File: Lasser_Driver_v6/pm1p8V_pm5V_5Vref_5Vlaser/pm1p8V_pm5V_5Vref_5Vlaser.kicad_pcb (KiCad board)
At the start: 2 copper layers, 160 x 100 mm, 103 parts, among them J6 DIN41612_M_3x8+8_Power_Male, U1 MC7808CTG, U10 LT3042EMSE +14.3V, U13 MC7812CTG, U14 MC7808CTG, U15 LT3045EMSE 5V, U16 LT3045EMSE 5V, U17 MC7808CTG, U18 MC7906CTG, U19 LT3045EMSE 5V, U2 LT3042EMSE +5.5V, U20 LT3094EMSE -5V, U21 OPA192IDBVR, U3 LTC6655BHMS8-5#PBF, U4 MC7812CTG, U5 MC7805CTG, U6 LT3045EMSE 3.3V, U7 LP5907MFX-1.8, U8 TPS7A3901DSCR, U9 LT3094EMSE -14.3V

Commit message: Main updates to CH card v6
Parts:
- R42, R43: value 20m PCB Trace -> 20m 1%
- moved C73 8.01 mm to (91.5, 135.8), turned to 180 degrees
- moved C75 0.50 mm to (94.4, 136.8)
- moved R49 0.50 mm to (97.0, 136.8)
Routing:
- net -15V: track 59.9 -> 65.4 mm
- net Net-(U21-IN-): track 2.75 -> 5.29 mm
- net GND: vias 267 -> 270
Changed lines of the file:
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@@
 		(tags "resistor handsolder")
 		(property "Reference" "R50"
-			(at 0 -1.65 0)
+			(at 0.2 1.6 180)
 			(layer "F.SilkS")
 			(effects
@@
 			(unit
 				(name "A")
-				(pins "3" "2" "5" "4" "1")
+				(pins "3" "4" "5" "2" "1")
 			)
 		)
@@
 	(footprint "Capacitor_SMD:C_0805_2012Metric_Pad1.18x1.45mm_HandSolder"
 		(layer "F.Cu")
-		(at 94.9625 128.55)
+		(at 91.4625 135.75 180)
 		(descr "Capacitor SMD 0805 (2012 Metric), square (rectangular) end terminal, IPC-7351 nominal with elongated pad for handsoldering. (Body size source: IPC-SM-782 page 76, https://www.pcb-3d.com/wordpress/wp-content/uploads/ipc-sm-782a_amendment_1_and_2.pdf, https://docs.google.com/spreadsheets/d/1BsfQQcO9C6DZCsRaXUlFlo91Tg2WpOkGARC1WS5S8t0/edit?usp=sharing)")
 		(tags "capacitor handsolder")
@@
 		)
 		(property "Manufacturer Part Number" "CL21B104KBCNNNC"
-			(at 0 0 0)
+			(at 0 0 180)
 			(unlocked yes)
 			(layer "F.Fab")
@@
 		)
 		(property "Manufacturer" "Samsung Electro-Mechanics"
-			(at 0 0 0)
+			(at 0 0 180)
 			(unlocked yes)
 			(layer "F.Fab")
@@
 		)
 		(property "DigiKey P/N" "1276-1003-2-ND"
-			(at 0 0 0)
+			(at 0 0 180)
 			(unlocked yes)
 			(layer "F.Fab")
@@
 		(duplicate_pad_numbers_are_jumpers no)
 		(fp_line
-			(start -0.261252 -0.735)
-			(end 0.261252 -0.735)
+			(start -0.261252 0.735)
+			(end 0.261252 0.735)
 			(stroke
 				(width 0.12)
@@
 		)
 		(fp_line
-			(start -0.261252 0.735)
-			(end 0.261252 0.735)
+			(start -0.261252 -0.735)
+			(end 0.261252 -0.735)
 			(stroke
 				(width 0.12)
@@
 		)
 		(pad "1" smd roundrect
-			(at -1.0375 0)
+			(at -1.0375 0 180)
 			(size 1.175 1.45)
 			(layers "F.Cu" "F.Mask" "F.Paste")
@@
 		)
 		(pad "2" smd roundrect
-			(at 1.0375 0)
+			(at 1.0375 0 180)
 			(size 1.175 1.45)
 			(layers "F.Cu" "F.Mask" "F.Paste")
@@
 			)
 		)
-		(property "Value" "20m PCB Trace"
+		(property "Value" "20m 1%"
 			(at 0 1.65 0)
 			(layer "F.Fab")
@@
 			)
 		)
+		(property "Manufacturer Part Number" "ERJ-6BWFR020V"
+			(at 0 0 180)
+			(unlocked yes)
+			(layer "F.Fab")
+			(hide yes)
+			(effects
+				(font
+					(size 1 1)
+					(thickness 0.15)
+				)
+			)
+		)
+		(property "Manufacturer" "Panasonic Industry"
+			(at 0 0 180)
+			(unlocked yes)
+			(layer "F.Fab")
+			(hide yes)
+			(effects
+				(font
+					(size 1 1)
+					(thickness 0.15)
+				)
+			)
+		)
+		(property "DigiKey P/N" "P.02AQTR-ND"
+			(at 0 0 180)
+			(unlocked yes)
+			(layer "F.Fab")
+			(hide yes)
+			(effects
+				(font
+					(size 1 1)
+					(thickness 0.15)
+				)
+			)
+		)
 		(sheetname "/")
 		(sheetfile "pm1p8V_pm5V_5Vref_5Vlaser.kicad_sch")
@@
 			)
 		)
-		(attr smd dnp)
+		(attr smd)
 		(duplicate_pad_numbers_are_jumpers no)
 		(fp_line
@@
 			)
 		)
-		(property "Value" "20m PCB Trace"
+		(property "Value" "20m 1%"
 			(at 0 1.65 0)
 			(layer "F.Fab")
@@
 			)
 		)
+		(property "Manufacturer Part Number" "ERJ-6BWFR020V"
+			(at 0 0 180)
+			(unlocked yes)
+			(layer "F.Fab")
+			(hide yes)
+			(effects
+				(font
+					(size 1 1)
+					(thickness 0.15)
+				)
+			)
+		)
+		(property "Manufacturer" "Panasonic Industry"
+			(at 0 0 180)
+			(unlocked yes)
+			(layer "F.Fab")
+			(hide yes)
+			(effects
+				(font
+					(size 1 1)
+					(thickness 0.15)
+				)
+			)
+		)
+		(property "DigiKey P/N" "P.02AQTR-ND"
+			(at 0 0 180)
+			(unlocked yes)
+			(layer "F.Fab")
+			(hide yes)
+			(effects
+				(font
+					(size 1 1)
+					(thickness 0.15)
+				)
+			)
+		)
 		(sheetname "/")
 		(sheetfile "pm1p8V_pm5V_5Vref_5Vlaser.kicad_sch")
@@
 			)
 		)
-		(attr smd dnp)
+		(attr smd)
 		(duplicate_pad_numbers_are_jumpers no)
 		(fp_line
@@
 	(footprint "Capacitor_SMD:C_0805_2012Metric_Pad1.18x1.45mm_HandSolder"
 		(layer "F.Cu")
-		(at 93.9 136.8125 -90)
+		(at 94.4 136.8125 -90)
 		(descr "Capacitor SMD 0805 (2012 Metric), square (rectangular) end terminal, IPC-7351 nominal with elongated pad for handsoldering. (Body size source: IPC-SM-782 page 76, https://www.pcb-3d.com/wordpress/wp-content/uploads/ipc-sm-782a_amendment_1_and_2.pdf, https://docs.google.com/spreadsheets/d/1BsfQQcO9C6DZCsRaXUlFlo91Tg2WpOkGARC1WS5S8t0/edit?usp=sharing)")
 		(tags "capacitor handsolder")
@@
 	(footprint "Resistor_SMD:R_0805_2012Metric_Pad1.20x1.40mm_HandSolder"
 		(layer "F.Cu")
-		(at 96.5 136.75 90)
+		(at 97 136.75 90)
 		(descr "Resistor SMD 0805 (2012 Metric), square (rectangular) end terminal, IPC-7351 nominal with elongated pad for handsoldering. (Body size source: IPC-SM-782 page 72, https://www.pcb-3d.com/wordpress/wp-content/uploads/ipc-sm-782a_amendment_1_and_2.pdf)")
 		(tags "resistor handsolder")
@@
 		(tags "capacitor handsolder")
 		(property "Reference" "C18"
-			(at 3.4375 0 90)
+			(at -0.8125 -1.65 90)
 			(layer "F.SilkS")
 			(effects
@@
 	)
 	(via
-		(at 91.5 140.1)
+		(at 94.4 139.4)
 		(size 0.8)
 		(drill 0.4)
@@
 	)
 	(via
+		(at 90.45 137.55)
+		(size 0.8)
+		(drill 0.4)
+		(layers "F.Cu" "B.Cu")
+		(free yes)
+		(net "GND")
+	)
+	(via
 		(at 203.8 107.5)
 		(size 0.8)
@@
 	)
 	(via
+		(at 90.45 126.65)
+		(size 0.8)
+		(drill 0.4)
+		(layers "F.Cu" "B.Cu")
+		(free yes)
+		(net "GND")
+	)
+	(via
 		(at 90.7 51.8)
 		(size 0.8)
@@
 	)
 	(via
-		(at 98.2 138.6)
+		(at 98.8 139.1)
 		(size 0.8)
 		(drill 0.4)
@@
 	)
 	(via
-		(at 96.5 139.6)
+		(at 97 139.3)
 		(size 0.8)
 		(drill 0.4)
@@
 	)
 	(via
+		(at 88.85 136)
+		(size 0.8)
+		(drill 0.4)
+		(layers "F.Cu" "B.Cu")
+		(free yes)
+		(net "GND")
+	)
+	(via
 		(at 152.8 107.7)
 		(size 0.8)
@@
 	)
 	(via
-		(at 93.9 139.6)
+		(at 95.75 137.8)
 		(size 0.8)
 		(drill 0.4)
@@
 	)
 	(via
-		(at 92.1 137.8)
+		(at 95.75 139.35)
 		(size 0.8)
 		(drill 0.4)
@@
 	)
 	(segment
-		(start 93.925 128.55)
-		(end 93.925 130.725)
-		(width 1)
-		(layer "F.Cu")
-		(net "-15V")
-	)
-	(segment
-		(start 93.1 126.4)
-		(end 85.2 126.4)
-		(width 1)
-		(layer "F.Cu")
-		(net "-15V")
-	)
-	(segment
 		(start 74.035 115.115)
 		(end 74.035 115.765)
@@
 	)
 	(segment
-		(start 85.2 126.4)
-		(end 84.5 125.7)
-		(width 1)
-		(layer "F.Cu")
-		(net "-15V")
-	)
-	(segment
-		(start 93.925 130.725)
-		(end 93.9 130.75)
+		(start 58.4 102.8)
+		(end 59.86 101.34)
 		(width 1)
 		(layer "F.Cu")
@@
 	)
 	(segment
-		(start 58.4 102.8)
-		(end 59.86 101.34)
+		(start 71.8 116.4)
+		(end 74.02 116.4)
 		(width 1)
 		(layer "F.Cu")
@@
 	)
 	(segment
-		(start 71.8 116.4)
-		(end 74.02 116.4)
+		(start 92.55 135.8)
+		(end 92.5 135.75)
 		(width 1)
 		(layer "F.Cu")
@@
 	)
 	(segment
-		(start 93.925 128.55)
-		(end 93.925 127.225)
+		(start 92.55 137.6)
+		(end 92.55 135.8)
 		(width 1)
 		(layer "F.Cu")
@@
 	)
 	(segment
-		(start 93.925 127.225)
-		(end 93.1 126.4)
-		(width 1)
-		(layer "F.Cu")
-		(net "-15V")
-	)
-	(segment
 		(start 74.035 116.415)
 		(end 74.035 116.535)
@@
 	)
 	(segment
+		(start 92.95 133.45)
+		(end 92.95 135.3)
+		(width 0.6)
+		(layer "F.Cu")
+		(net "-15V")
+	)
+	(segment
 		(start 59.86 101.34)
 		(end 60.36 101.34)
@@
 	)
 	(via
-		(at 84.5 125.7)
+		(at 92.55 137.6)
 		(size 1)
 		(drill 0.5)
@@
 	(segment
 		(start 76.6 117.8)
-		(end 74.5 117.8)
+		(end 86.25 127.45)
 		(width 1)
 		(layer "B.Cu")
@@
 	)
 	(segment
-		(start 84.5 125.7)
+		(start 74.5 117.8)
 		(end 76.6 117.8)
 		(width 1)
@@
 	)
 	(segment
+		(start 92.2 137.6)
+		(end 92.55 137.6)
+		(width 1)
+		(layer "B.Cu")
+		(net "-15V")
+	)
+	(segment
+		(start 86.25 131.65)
+		(end 92.2 137.6)
+		(width 1)
+		(layer "B.Cu")
+		(net "-15V")
+	)
+	(segment
+		(start 86.25 127.45)
+		(end 86.25 131.65)
+		(width 1)
+		(layer "B.Cu")
+		(net "-15V")
+	)
+	(segment
 		(start 212.5 68.35)
 		(end 212.5 111.5)
@@
 	)
 	(segment
-		(start 96.5 135.75)
-		(end 93.925 135.75)
+		(start 97 135.75)
+		(end 94.425 135.75)
 		(width 0.25)
 		(layer "F.Cu")
@@
 	)
 	(segment
-		(start 92.95 133.45)
-		(end 92 133.45)
+		(start 92 132.65)
+		(end 93.9 130.75)
 		(width 0.25)
 		(layer "F.Cu")
@@
 	(segment
 		(start 92 133.45)
-		(end 90.2 133.45)
+		(end 92 132.65)
+		(width 0.25)
+		(layer "F.Cu")
+		(net "Net-(U21-IN-)")
+	)
+	(segment
+		(start 90.2 133.45)
+		(end 92 133.45)
 		(width 0.25)
 		(layer "F.Cu")

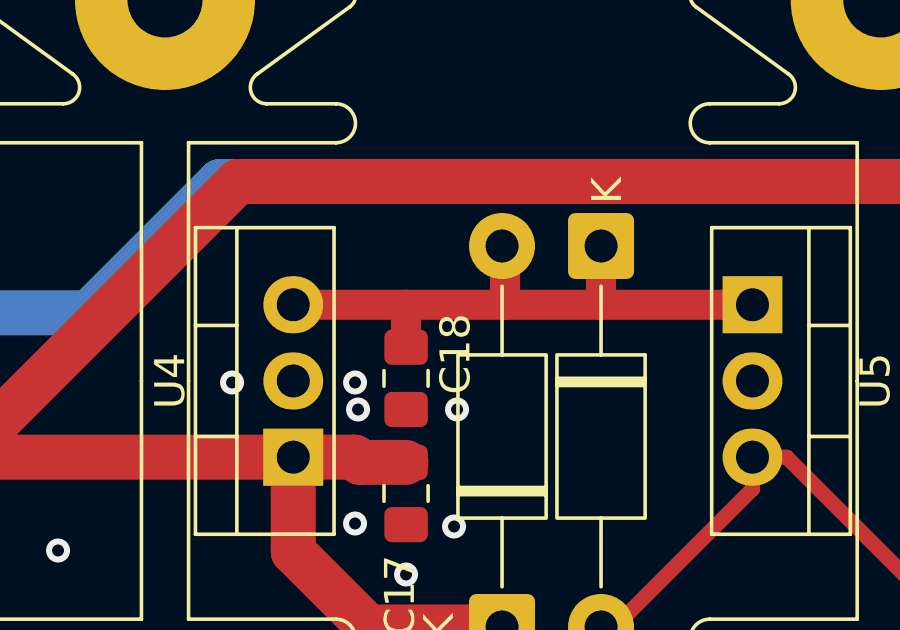
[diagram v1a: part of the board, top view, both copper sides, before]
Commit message: updates to AFE, CH, DIG and pm1p8_pm5V_5Vlaser
schematics and pcbs updated.  They seem to be ready, but will take one more look with fresh eyes before ordering.
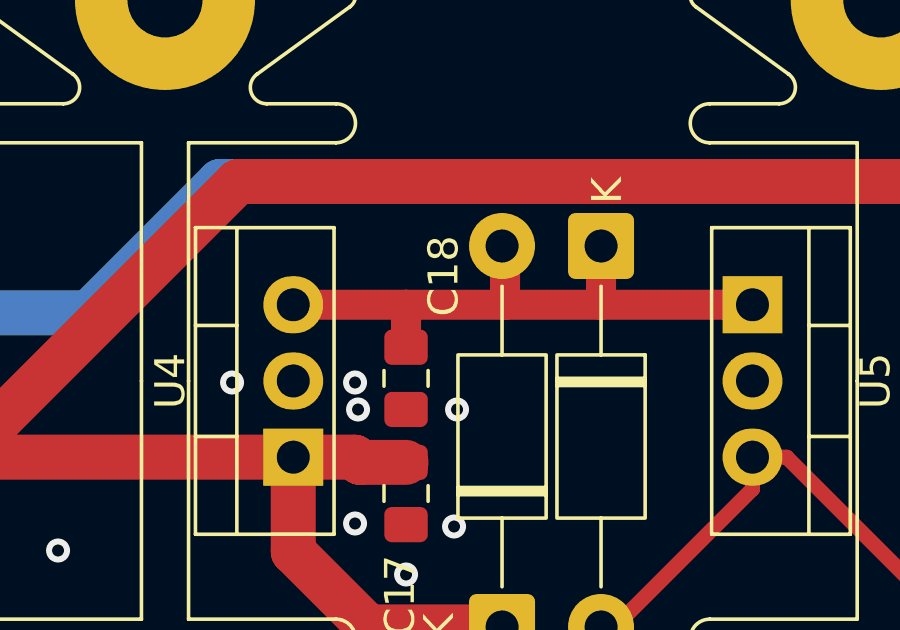
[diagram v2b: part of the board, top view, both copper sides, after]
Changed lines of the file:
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@@
 		(tags "capacitor handsolder")
 		(property "Reference" "C18"
-			(at -0.8125 -1.65 90)
+			(at -3.4125 -1.25 90)
 			(layer "F.SilkS")
 			(effects
